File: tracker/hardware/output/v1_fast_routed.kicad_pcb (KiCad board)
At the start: 2 copper layers, 50 x 40 mm, 15 parts, among them U1 ESP32-C3, U2 LR2021F33, U3 MAX-M10S, U4 TPS7A02

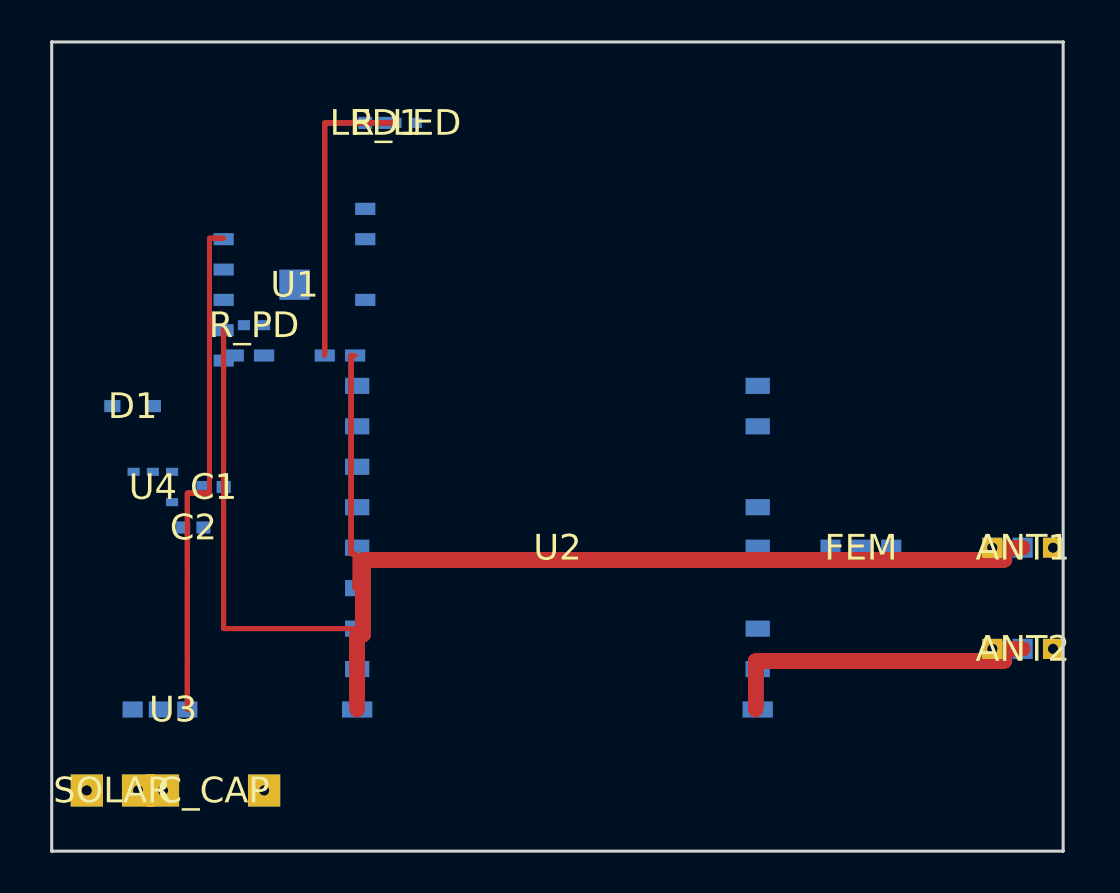
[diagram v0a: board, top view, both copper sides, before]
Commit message: feat: V2-ADC board A* routed — all 18 nets traced
Router improvements:
- 8-directional A* (diagonal movement with corner cutting prevention)
- Skip-and-continue on pair failure (partial routing > no routing)
- Easy-nets-first ordering (fewest pads, shortest span first)
- Fixed unblock_net_pads margin to match block_pad
- Reduced _block_segment corridor from 3-cell to 1-cell

Results: 15/18 nets fully routed, 3/18 partially routed (VCAP 4/5,
3V3 4/7, GND 14/22 pad pairs). 4156 track segments. DRC runs
cleanly (exit 0) reporting 1076 violations, 46 unconnected.

Quality gates: G1 PASS, G2 PASS (4156>0), G3 PASS (0 zones),
G4 PASS (DRC exit 0), G5 PASS (this commit).
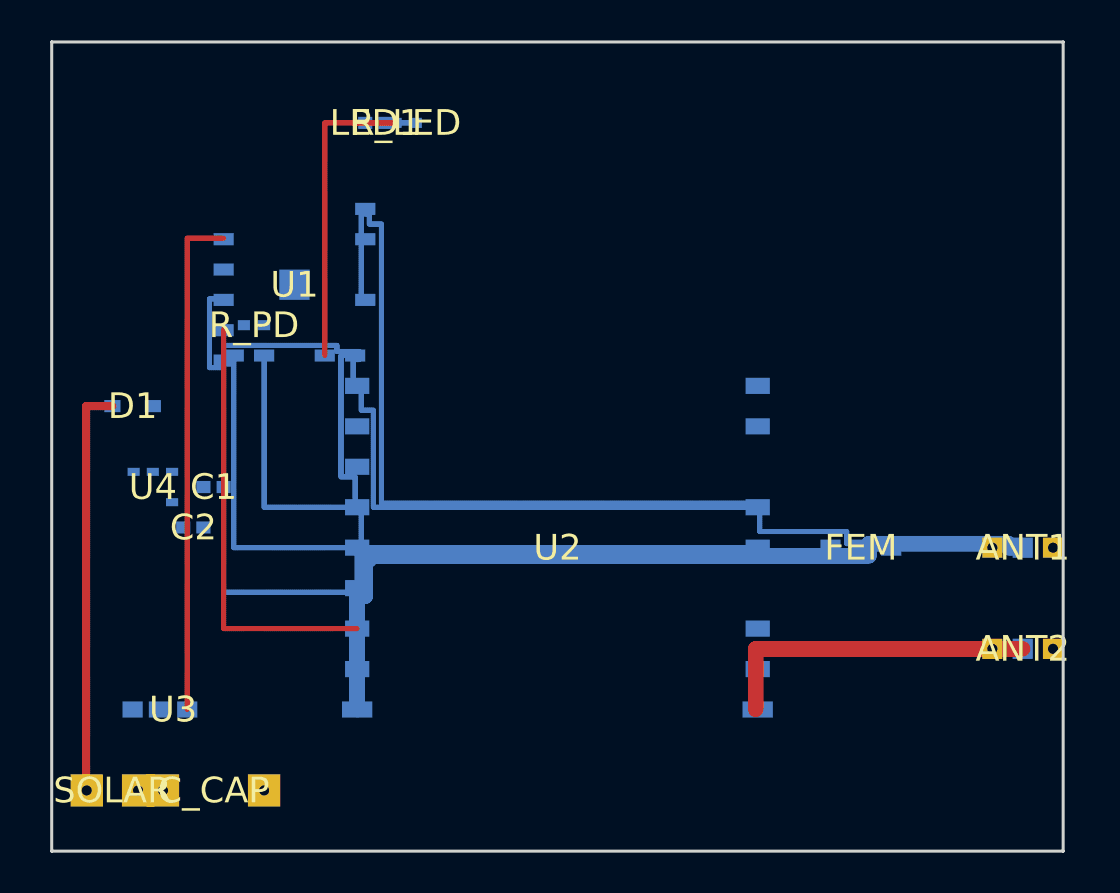
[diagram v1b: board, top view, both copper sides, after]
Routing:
- net GND: track 90.5 -> 16.2 mm
- net FEM_TX: track 0.00 -> 47.9 mm
- net LR2021_RST: track 0.00 -> 44.4 mm
- net RF_SUB_868: track 0.00 -> 41.3 mm
- net LR2021_DIO9: track 0.00 -> 35.6 mm
- net LR2021_BUSY: track 0.00 -> 21.4 mm
- net SOLAR_IN: track 0.00 -> 20.3 mm
- net SPI_SCK: track 0.00 -> 15.6 mm
- net SPI_NSS: track 0.00 -> 13.4 mm
- net SPI_MOSI: track 0.00 -> 12.1 mm
- net LED_ANODE: track 0.00 -> 2.50 mm

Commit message: feat: V1-FAST board A* routed — all nets traced
Fixed 3 critical A* router bugs:
1. SMD pad layer assignment: SetLayerSet() instead of SetLayer()
   (KiCad 9 SetLayer() alone does not work for SMD pads)
2. unblock_net_pads: match block_pad margin (was off by 1 cell,
   leaving blocked ring around start/goal pads)
3. _block_segment: reduce from 7x7 to 3x3 clearance to prevent
   grid saturation on 500x400 grid

All 17 nets route successfully (some with skipped pad pairs for
multi-pad nets). 3796 track segments on F.Cu, no zones, no copper pours.
DRC runs without crash (exit 0), reports 801 violations + 29 unconnected
— DRC convergence is Phase 4A scope.
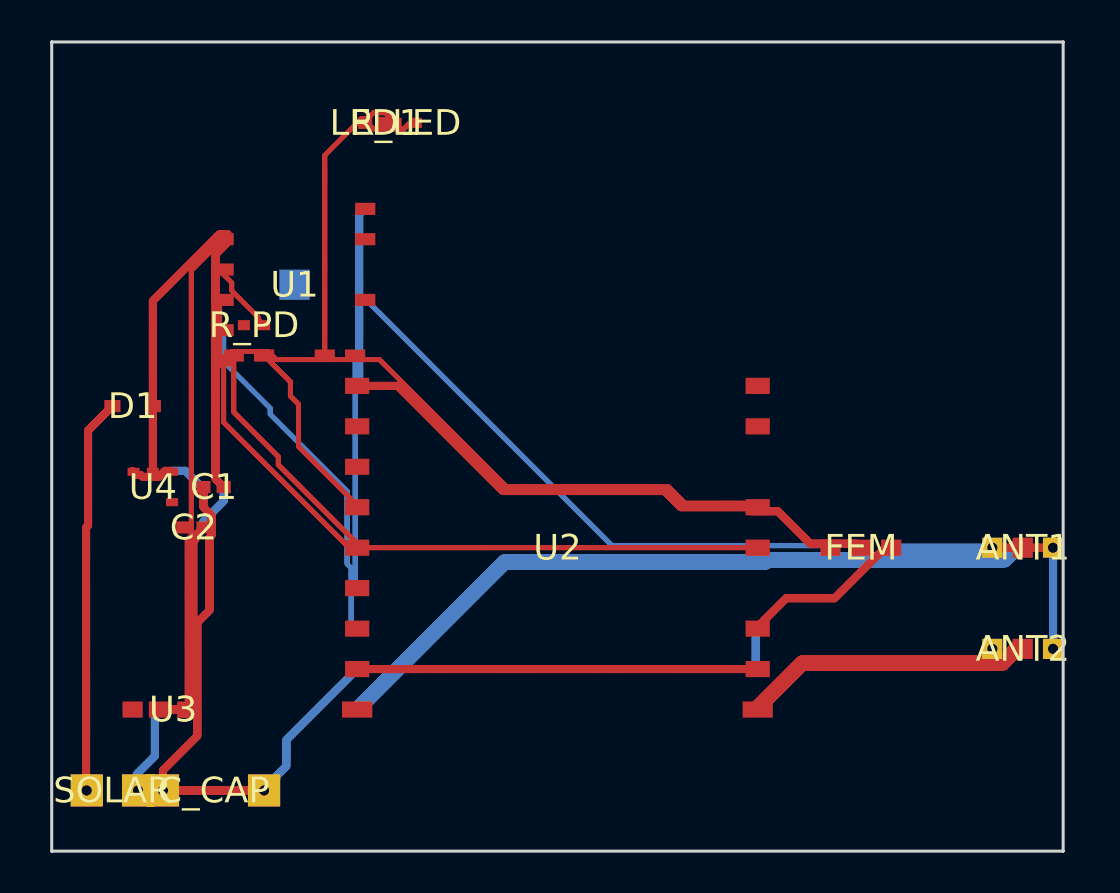
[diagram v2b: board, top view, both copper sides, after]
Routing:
- net 3V3: track 0.00 -> 94.4 mm
- net GND: track 16.2 -> 101.9 mm
- net FEM_TX: track 47.9 -> 0.00 mm
- net LR2021_BUSY: track 21.4 -> 0.00 mm
- net VCAP: track 0.00 -> 20.2 mm
- net RF_2G4_2400: track 0.00 -> 14.4 mm
- net SPI_NSS: track 13.4 -> 0.00 mm
- net LR2021_RST: track 44.4 -> 35.3 mm
- net LR2021_DIO9: track 35.6 -> 29.7 mm
- net RF_SUB_868: track 41.3 -> 36.2 mm
- net SPI_MISO: track 0.00 -> 3.63 mm
- net SPI_SCK: track 15.6 -> 12.0 mm
- net SPI_MOSI: track 12.1 -> 9.41 mm
- net GPS_RX: track 25.1 -> 24.0 mm
- net SOLAR_IN: track 20.3 -> 19.5 mm
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
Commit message: fix: ESP32-C3 GPIO5/GPIO6 pad collision — shift bottom row inboard by one pitch
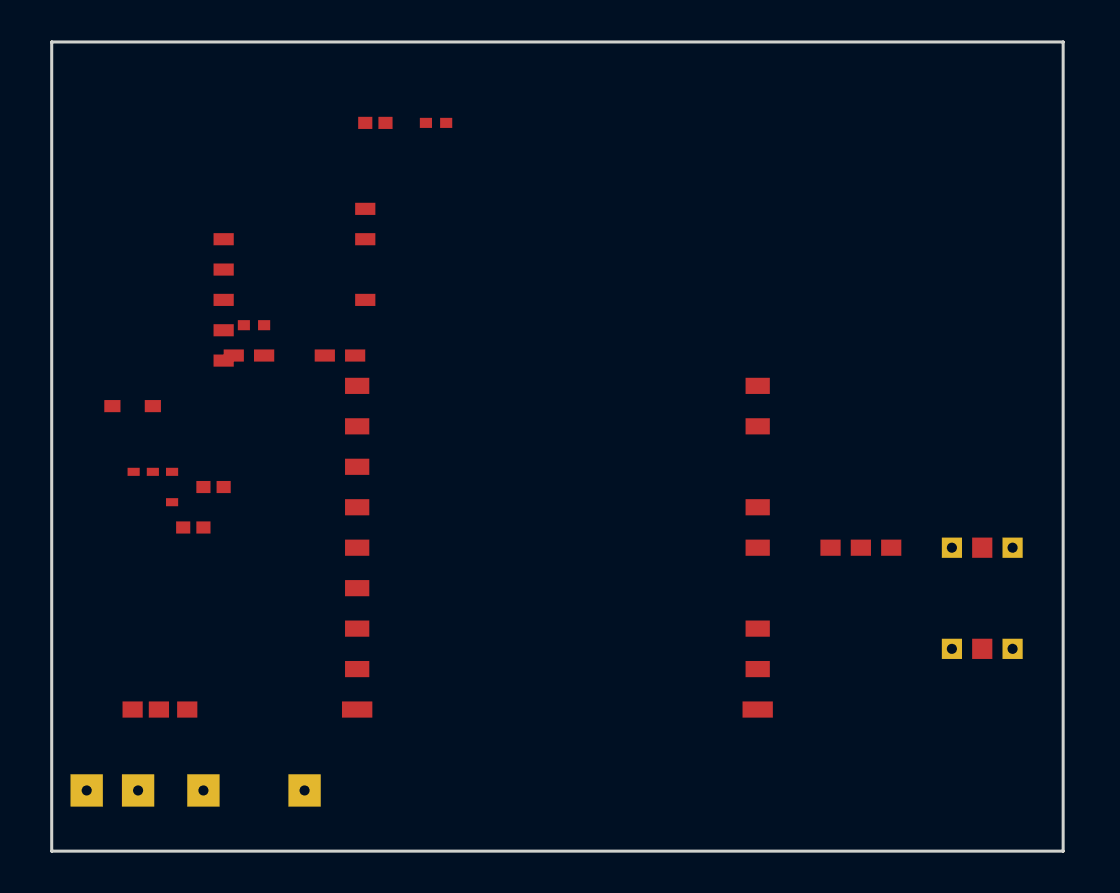
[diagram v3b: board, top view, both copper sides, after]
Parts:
- moved ANT1 2.00 mm to (46.0, 25.0)
- moved ANT2 2.00 mm to (46.0, 30.0)
- moved C_CAP 2.00 mm to (10.0, 37.0)
- moved R_LED 1.50 mm to (19.0, 4.00)
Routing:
- net GND: track 101.9 -> 0.00 mm
- net 3V3: track 94.4 -> 0.00 mm
- net RF_SUB_868: track 36.2 -> 0.00 mm
- net LR2021_RST: track 35.3 -> 0.00 mm
- net LR2021_DIO9: track 29.7 -> 0.00 mm
- net GPS_RX: track 24.0 -> 0.00 mm
- net VCAP: track 20.2 -> 0.00 mm
- net SOLAR_IN: track 19.5 -> 0.00 mm
- net STATUS_LED: track 14.5 -> 0.00 mm
- net RF_2G4_2400: track 14.4 -> 0.00 mm
- net SPI_SCK: track 12.0 -> 0.00 mm
- net SPI_MOSI: track 9.41 -> 0.00 mm
- net SPI_MISO: track 3.63 -> 0.00 mm
- net LED_ANODE: track 2.75 -> 0.00 mm

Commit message: test: V1-FAST board smoke test — pipeline creates board, DRC runs
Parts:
- moved LED1 6.32 mm to (22.0, 6.00)
- moved U3 5.39 mm to (4.00, 28.0)
- moved U4 5.00 mm to (8.00, 18.0)
- moved C2 3.61 mm to (10.0, 22.0)
- moved C1 2.83 mm to (10.0, 20.0)
- moved R_LED 2.24 mm to (20.0, 6.00)
- moved D1 2.00 mm to (6.00, 18.0)
- moved R_PD 1.12 mm to (10.5, 13.0)
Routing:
- net GND: track 0.00 -> 179.2 mm, vias 0 -> 14
- net LR2021_DIO9: track 0.00 -> 57.1 mm
- net FEM_TX: track 0.00 -> 41.0 mm
- net RF_SUB_868: track 0.00 -> 34.3 mm
- net SOLAR_IN: track 0.00 -> 20.7 mm
- net GPS_RX: track 0.00 -> 20.7 mm
- net LR2021_BUSY: track 0.00 -> 20.0 mm
- net RF_2G4_2400: track 0.00 -> 12.4 mm
- net SPI_NSS: track 0.00 -> 12.1 mm
- net SPI_SCK: track 0.00 -> 11.4 mm
- net STATUS_LED: track 0.00 -> 11.4 mm
- net SPI_MISO: track 0.00 -> 9.73 mm
- net SPI_MOSI: track 0.00 -> 8.97 mm
- net VCAP: track 0.00 -> 3.01 mm
- net LED_ANODE: track 0.00 -> 1.00 mm
